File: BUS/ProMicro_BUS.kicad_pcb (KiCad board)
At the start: 2 copper layers, 17.8 x 30.5 mm, 17 parts, among them J1 Conn_01x03, U1 MAX3483, U2 MCP2515-xSO, U3 MAX3051, Y1 Crystal

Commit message: dump
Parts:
- removed the C1 at (53.3, 87.0)
- removed the C4 at (55.2, 87.0)
- removed C5, C6: 100n, Capacitor_SMD:C_0603_1608Metric
- added C2: 100n, Capacitor_SMD:C_0402_1005Metric, F.Cu at (55.2, 86.4)
- added C3: 10µ, Capacitor_SMD:C_0603_1608Metric, F.Cu at (53.3, 87.0)
- A1: value Sparkfun_Pro_Micro_3V3 -> Sparkfun_Pro_Micro
- moved LOGO1 10.4 mm to (59.1, 100.3), turned to 90 degrees
- moved JP3 2.57 mm to (57.2, 104.1)
- renumbered C2 to C1, C3 to C4, JP2 to JP1, JP1 to JP2, U3 to U2, U2 to U3
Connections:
- net D0 renamed TXD
- net D1 renamed RXD
- net D14 renamed CIPO
- net D15 renamed SCK
- net D16 renamed COPI
- net D7 renamed INT
- net D9 renamed CS1
- net Reset renamed ~RST
- A1 pad 13: (no net) -> CS0
- A1 pad 8: D5 -> (no net)
- JP3 pad 1: D5 -> CS0
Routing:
- net D5: track 24.1 -> 0.00 mm
- net CS0: track 0.00 -> 7.56 mm
- net CS1: track 2.51 -> 5.08 mm
- net CS: track 17.6 -> 16.6 mm
- net +3V3: track 26.1 -> 27.0 mm
- net GND: vias 26 -> 24
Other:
- board text added: "A"
- board text added: "B"
- board text added: "CIPO"
- board text added: "COPI"
- board text added: "CS0"
- board text added: "CS1"
- board text added: "G"
- board text added: "nerdyscout.github.io/ ProMicro/BUS v1.3"
- board text added: "~RST"
- board text removed: "CS"
- board text removed: "MISO"
- board text removed: "MOSI"
- board text removed: "RESET"
- board text removed: "TXDEN"
- board text removed: "nerdyscout.github.io/ProMicro/BUS"
- board text removed: "v1.2"

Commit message: clean
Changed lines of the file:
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@@
-(kicad_pcb (version 20171130) (host pcbnew 5.1.5)
+(kicad_pcb (version 20171130) (host pcbnew 5.1.5+dfsg1-2build2)
   (general
     (thickness 0.8)
     (drawings 24)
-    (tracks 178)
+    (tracks 179)
     (zones 0)
     (modules 15)
@@
       (effects (font (size 1 1) (thickness 0.15)))
     )
-    (pad 1 thru_hole rect (at 0 0) (size 1.6 1.6) (drill 0.8) (layers *.Cu *.Mask)
+    (pad 1 thru_hole rect (at 0 0) (size 2 2) (drill 1) (layers *.Cu *.Mask)
       (net 10 RXD))
-    (pad 2 thru_hole oval (at 0 2.54) (size 1.6 1.6) (drill 0.8) (layers *.Cu *.Mask)
+    (pad 2 thru_hole oval (at 0 2.54) (size 2 2) (drill 1) (layers *.Cu *.Mask)
       (net 11 TXD))
-    (pad 3 thru_hole oval (at 0 5.08) (size 1.6 1.6) (drill 0.8) (layers *.Cu *.Mask)
+    (pad 3 thru_hole oval (at 0 5.08) (size 2 2) (drill 1) (layers *.Cu *.Mask)
       (net 1 GND))
-    (pad 13 thru_hole oval (at 15.24 27.94) (size 1.6 1.6) (drill 0.8) (layers *.Cu *.Mask)
+    (pad 13 thru_hole oval (at 15.24 27.94) (size 2 2) (drill 1) (layers *.Cu *.Mask)
       (net 12 CS0))
-    (pad 4 thru_hole oval (at 0 7.62) (size 1.6 1.6) (drill 0.8) (layers *.Cu *.Mask)
+    (pad 4 thru_hole oval (at 0 7.62) (size 2 2) (drill 1) (layers *.Cu *.Mask)
       (net 1 GND))
-    (pad 14 thru_hole oval (at 15.24 25.4) (size 1.6 1.6) (drill 0.8) (layers *.Cu *.Mask)
+    (pad 14 thru_hole oval (at 15.24 25.4) (size 2 2) (drill 1) (layers *.Cu *.Mask)
       (net 13 COPI))
-    (pad 5 thru_hole oval (at 0 10.16) (size 1.6 1.6) (drill 0.8) (layers *.Cu *.Mask))
-    (pad 15 thru_hole oval (at 15.24 22.86) (size 1.6 1.6) (drill 0.8) (layers *.Cu *.Mask)
+    (pad 5 thru_hole oval (at 0 10.16) (size 2 2) (drill 1) (layers *.Cu *.Mask))
+    (pad 15 thru_hole oval (at 15.24 22.86) (size 2 2) (drill 1) (layers *.Cu *.Mask)
       (net 14 CIPO))
-    (pad 6 thru_hole oval (at 0 12.7) (size 1.6 1.6) (drill 0.8) (layers *.Cu *.Mask))
-    (pad 16 thru_hole oval (at 15.24 20.32) (size 1.6 1.6) (drill 0.8) (layers *.Cu *.Mask)
+    (pad 6 thru_hole oval (at 0 12.7) (size 2 2) (drill 1) (layers *.Cu *.Mask))
+    (pad 16 thru_hole oval (at 15.24 20.32) (size 2 2) (drill 1) (layers *.Cu *.Mask)
       (net 15 SCK))
-    (pad 7 thru_hole oval (at 0 15.24) (size 1.6 1.6) (drill 0.8) (layers *.Cu *.Mask))
-    (pad 17 thru_hole oval (at 15.24 17.78) (size 1.6 1.6) (drill 0.8) (layers *.Cu *.Mask))
-    (pad 8 thru_hole oval (at 0 17.78) (size 1.6 1.6) (drill 0.8) (layers *.Cu *.Mask))
-    (pad 18 thru_hole oval (at 15.24 15.24) (size 1.6 1.6) (drill 0.8) (layers *.Cu *.Mask))
-    (pad 9 thru_hole oval (at 0 20.32) (size 1.6 1.6) (drill 0.8) (layers *.Cu *.Mask))
-    (pad 19 thru_hole oval (at 15.24 12.7) (size 1.6 1.6) (drill 0.8) (layers *.Cu *.Mask))
-    (pad 10 thru_hole oval (at 0 22.86) (size 1.6 1.6) (drill 0.8) (layers *.Cu *.Mask)
+    (pad 7 thru_hole oval (at 0 15.24) (size 2 2) (drill 1) (layers *.Cu *.Mask))
+    (pad 17 thru_hole oval (at 15.24 17.78) (size 2 2) (drill 1) (layers *.Cu *.Mask))
+    (pad 8 thru_hole oval (at 0 17.78) (size 2 2) (drill 1) (layers *.Cu *.Mask))
+    (pad 18 thru_hole oval (at 15.24 15.24) (size 2 2) (drill 1) (layers *.Cu *.Mask))
+    (pad 9 thru_hole oval (at 0 20.32) (size 2 2) (drill 1) (layers *.Cu *.Mask))
+    (pad 19 thru_hole oval (at 15.24 12.7) (size 2 2) (drill 1) (layers *.Cu *.Mask))
+    (pad 10 thru_hole oval (at 0 22.86) (size 2 2) (drill 1) (layers *.Cu *.Mask)
       (net 16 INT))
-    (pad 20 thru_hole oval (at 15.24 10.16) (size 1.6 1.6) (drill 0.8) (layers *.Cu *.Mask))
-    (pad 11 thru_hole oval (at 0 25.4) (size 1.6 1.6) (drill 0.8) (layers *.Cu *.Mask))
-    (pad 21 thru_hole oval (at 15.24 7.62) (size 1.6 1.6) (drill 0.8) (layers *.Cu *.Mask)
+    (pad 20 thru_hole oval (at 15.24 10.16) (size 2 2) (drill 1) (layers *.Cu *.Mask))
+    (pad 11 thru_hole oval (at 0 25.4) (size 2 2) (drill 1) (layers *.Cu *.Mask))
+    (pad 21 thru_hole oval (at 15.24 7.62) (size 2 2) (drill 1) (layers *.Cu *.Mask)
       (net 2 +3V3))
-    (pad 12 thru_hole oval (at 0 27.94) (size 1.6 1.6) (drill 0.8) (layers *.Cu *.Mask)
+    (pad 12 thru_hole oval (at 0 27.94) (size 2 2) (drill 1) (layers *.Cu *.Mask)
       (net 17 CS1))
-    (pad 22 thru_hole oval (at 15.24 5.08) (size 1.6 1.6) (drill 0.8) (layers *.Cu *.Mask)
+    (pad 22 thru_hole oval (at 15.24 5.08) (size 2 2) (drill 1) (layers *.Cu *.Mask)
       (net 18 ~RST))
-    (pad 23 thru_hole oval (at 15.24 2.54) (size 1.6 1.6) (drill 0.8) (layers *.Cu *.Mask)
+    (pad 23 thru_hole oval (at 15.24 2.54) (size 2 2) (drill 1) (layers *.Cu *.Mask)
       (net 1 GND))
-    (pad 24 thru_hole oval (at 15.24 0) (size 1.6 1.6) (drill 0.8) (layers *.Cu *.Mask))
+    (pad 24 thru_hole oval (at 15.24 0) (size 2 2) (drill 1) (layers *.Cu *.Mask))
     (model ${KISYS3DMOD}/Module.3dshapes/Sparkfun_Pro_Micro.wrl
       (at (xyz 0 0 0))
@@
   (via (at 56.515 87.249) (size 0.6) (drill 0.3) (layers F.Cu B.Cu) (net 2))
   (segment (start 56.515 92.075) (end 56.515 87.249) (width 0.4) (layer B.Cu) (net 2))
-  (segment (start 60.556 87.48) (end 60.556 87.48) (width 0.4) (layer F.Cu) (net 2))
   (segment (start 55.245 87.7825) (end 54.2545 87.7825) (width 0.4) (layer F.Cu) (net 2))
   (segment (start 63.5 88.9) (end 63.5 88.9) (width 0.4) (layer F.Cu) (net 2))
@@
   (segment (start 62.507 87.757) (end 61.595 87.757) (width 0.4) (layer F.Cu) (net 2))
   (segment (start 62.507 87.757) (end 63.5 87.757) (width 0.4) (layer F.Cu) (net 2))
-  (segment (start 63.5 87.7825) (end 63.5 88.9) (width 0.4) (layer F.Cu) (net 2))
-  (segment (start 64.77 85.09) (end 66.04 83.82) (width 0.4) (layer F.Cu) (net 2))
-  (segment (start 64.2365 87.7825) (end 64.77 87.249) (width 0.4) (layer F.Cu) (net 2))
-  (segment (start 63.5 87.7825) (end 64.2365 87.7825) (width 0.4) (layer F.Cu) (net 2))
-  (segment (start 64.77 87.249) (end 64.77 85.09) (width 0.4) (layer F.Cu) (net 2))
   (via (at 60.579 87.249012) (size 0.6) (drill 0.3) (layers F.Cu B.Cu) (net 2))
   (segment (start 60.324988 86.995) (end 60.329001 86.999013) (width 0.4) (layer F.Cu) (net 2))
-  (segment (start 61.112488 87.7825) (end 60.579 87.249012) (width 0.4) (layer F.Cu) (net 2))
   (segment (start 58.7375 86.995) (end 60.324988 86.995) (width 0.4) (layer F.Cu) (net 2))
-  (segment (start 61.595 87.7825) (end 61.112488 87.7825) (width 0.4) (layer F.Cu) (net 2))
   (segment (start 60.329001 86.999013) (end 60.579 87.249012) (width 0.4) (layer F.Cu) (net 2))
   (segment (start 55.245 86.845) (end 55.245 86.995) (width 0.4) (layer F.Cu) (net 2))
   (segment (start 55.245 86.995) (end 55.245 87.7825) (width 0.4) (layer F.Cu) (net 2))
+  (segment (start 64.516 87.503) (end 64.516 85.344) (width 0.4) (layer F.Cu) (net 2))
+  (segment (start 64.262 87.757) (end 64.516 87.503) (width 0.4) (layer F.Cu) (net 2))
+  (segment (start 63.5 87.757) (end 64.262 87.757) (width 0.4) (layer F.Cu) (net 2))
+  (segment (start 64.516 85.344) (end 66.04 83.82) (width 0.4) (layer F.Cu) (net 2))
+  (segment (start 63.5 88.9) (end 63.5 87.757) (width 0.4) (layer F.Cu) (net 2))
+  (segment (start 61.086988 87.757) (end 60.579 87.249012) (width 0.4) (layer F.Cu) (net 2))
+  (segment (start 61.5695 87.757) (end 61.086988 87.757) (width 0.4) (layer F.Cu) (net 2))
   (segment (start 58.75 85.115) (end 58.75 85.895) (width 0.25) (layer F.Cu) (net 3))
   (segment (start 59.2075 83.82) (end 59.2075 84.6575) (width 0.25) (layer F.Cu) (net 3))
@@
   (segment (start 53.31 104.14) (end 50.8 104.14) (width 0.25) (layer B.Cu) (net 17))
   (segment (start 55.88 104.14) (end 53.31 104.14) (width 0.25) (layer B.Cu) (net 17))
-  (via (at 64.77 90.17) (size 0.5) (drill 0.2) (layers F.Cu B.Cu) (net 18))
-  (segment (start 64.77 90.17) (end 64.77 82.55) (width 0.25) (layer B.Cu) (net 18))
-  (segment (start 64.77 82.55) (end 66.04 81.28) (width 0.25) (layer B.Cu) (net 18))
-  (segment (start 64.77 91.059) (end 64.77 90.17) (width 0.25) (layer F.Cu) (net 18))
+  (via (at 64.515992 90.805) (size 0.5) (drill 0.2) (layers F.Cu B.Cu) (net 18))
+  (segment (start 66.04 81.28) (end 64.515992 82.804008) (width 0.25) (layer B.Cu) (net 18))
+  (segment (start 64.515992 82.804008) (end 64.515992 90.451447) (width 0.25) (layer B.Cu) (net 18))
+  (segment (start 64.515992 90.451447) (end 64.515992 90.805) (width 0.25) (layer B.Cu) (net 18))
+  (segment (start 64.515992 91.312992) (end 64.515992 90.805) (width 0.25) (layer F.Cu) (net 18))
+  (segment (start 64.516 91.313) (end 64.515992 91.312992) (width 0.25) (layer F.Cu) (net 18))
+  (segment (start 64.389 91.44) (end 64.516 91.313) (width 0.25) (layer F.Cu) (net 18))
   (segment (start 63.07 91.44) (end 64.389 91.44) (width 0.25) (layer F.Cu) (net 18))
-  (segment (start 64.389 91.44) (end 64.77 91.059) (width 0.25) (layer F.Cu) (net 18))
   (segment (start 56.57 103.378) (end 54.483 103.378) (width 0.25) (layer F.Cu) (net 19))
   (segment (start 53.77 99.06) (end 55.372 99.06) (width 0.25) (layer F.Cu) (net 19))

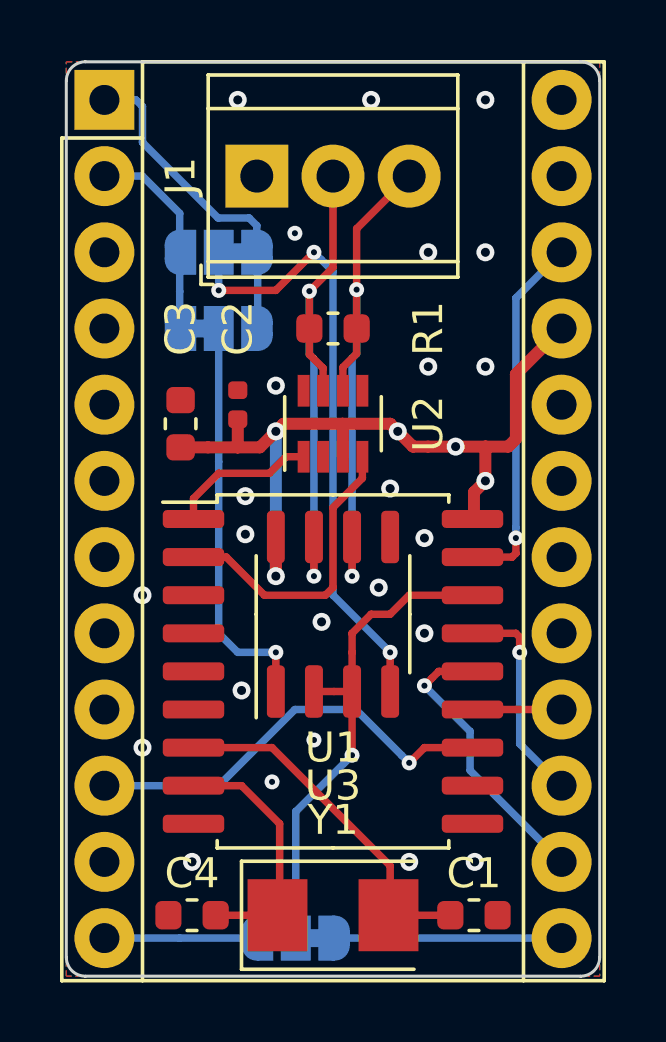
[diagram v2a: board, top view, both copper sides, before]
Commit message: make controller holes wide enough
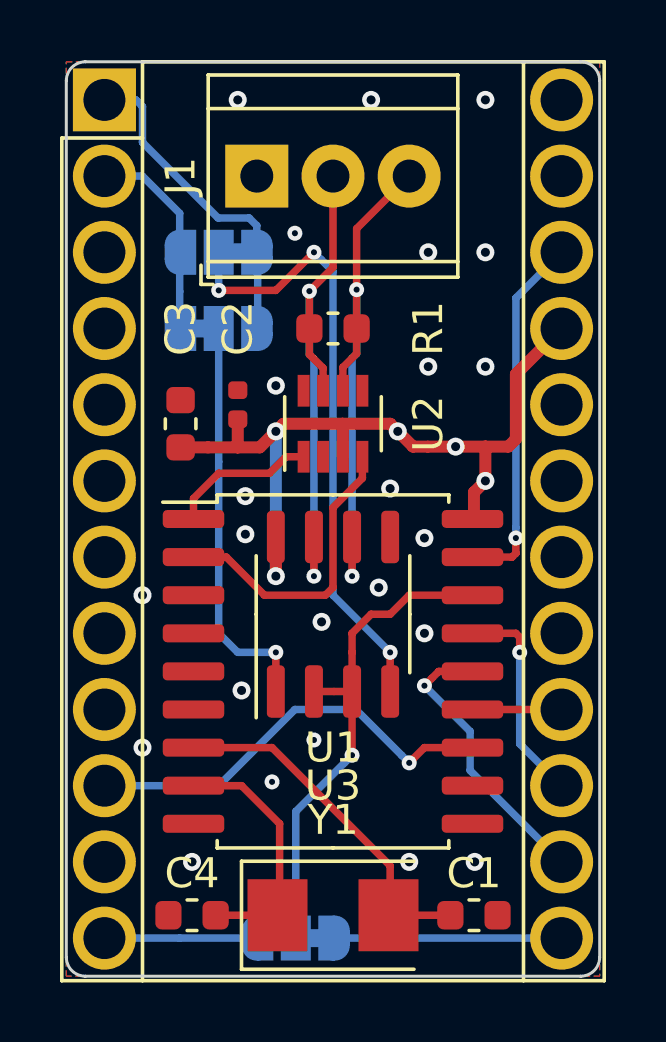
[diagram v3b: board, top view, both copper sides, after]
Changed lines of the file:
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@@
-(kicad_pcb (version 20171130) (host pcbnew 5.1.5+dfsg1-2build2)
+(kicad_pcb (version 20171130) (host pcbnew 5.1.5)
   (general
     (thickness 0.8)
@@
       (effects (font (size 1 1) (thickness 0.15)))
     )
-    (pad 1 thru_hole rect (at 0 0) (size 2 2) (drill 1) (layers *.Cu *.Mask)
+    (pad 1 thru_hole rect (at 0 0) (size 2.1 2.1) (drill 1.4) (layers *.Cu *.Mask)
       (net 10 RXD))
-    (pad 2 thru_hole oval (at 0 2.54) (size 2 2) (drill 1) (layers *.Cu *.Mask)
+    (pad 2 thru_hole circle (at 0 2.54) (size 2.1 2.1) (drill 1.4) (layers *.Cu *.Mask)
       (net 11 TXD))
-    (pad 3 thru_hole oval (at 0 5.08) (size 2 2) (drill 1) (layers *.Cu *.Mask)
-      (net 1 GND))
-    (pad 13 thru_hole oval (at 15.24 27.94) (size 2 2) (drill 1) (layers *.Cu *.Mask)
+    (pad 3 thru_hole circle (at 0 5.08) (size 2.1 2.1) (drill 1.4) (layers *.Cu *.Mask)
+      (net 1 GND))
+    (pad 13 thru_hole circle (at 15.24 27.94) (size 2.1 2.1) (drill 1.4) (layers *.Cu *.Mask)
       (net 12 CS0))
-    (pad 4 thru_hole oval (at 0 7.62) (size 2 2) (drill 1) (layers *.Cu *.Mask)
-      (net 1 GND))
-    (pad 14 thru_hole oval (at 15.24 25.4) (size 2 2) (drill 1) (layers *.Cu *.Mask)
+    (pad 4 thru_hole circle (at 0 7.62) (size 2.1 2.1) (drill 1.4) (layers *.Cu *.Mask)
+      (net 1 GND))
+    (pad 14 thru_hole circle (at 15.24 25.4) (size 2.1 2.1) (drill 1.4) (layers *.Cu *.Mask)
       (net 13 COPI))
-    (pad 5 thru_hole oval (at 0 10.16) (size 2 2) (drill 1) (layers *.Cu *.Mask))
-    (pad 15 thru_hole oval (at 15.24 22.86) (size 2 2) (drill 1) (layers *.Cu *.Mask)
+    (pad 5 thru_hole circle (at 0 10.16) (size 2.1 2.1) (drill 1.4) (layers *.Cu *.Mask))
+    (pad 15 thru_hole circle (at 15.24 22.86) (size 2.1 2.1) (drill 1.4) (layers *.Cu *.Mask)
       (net 14 CIPO))
-    (pad 6 thru_hole oval (at 0 12.7) (size 2 2) (drill 1) (layers *.Cu *.Mask))
-    (pad 16 thru_hole oval (at 15.24 20.32) (size 2 2) (drill 1) (layers *.Cu *.Mask)
+    (pad 6 thru_hole circle (at 0 12.7) (size 2.1 2.1) (drill 1.4) (layers *.Cu *.Mask))
+    (pad 16 thru_hole circle (at 15.24 20.32) (size 2.1 2.1) (drill 1.4) (layers *.Cu *.Mask)
       (net 15 SCK))
-    (pad 7 thru_hole oval (at 0 15.24) (size 2 2) (drill 1) (layers *.Cu *.Mask))
-    (pad 17 thru_hole oval (at 15.24 17.78) (size 2 2) (drill 1) (layers *.Cu *.Mask))
-    (pad 8 thru_hole oval (at 0 17.78) (size 2 2) (drill 1) (layers *.Cu *.Mask))
-    (pad 18 thru_hole oval (at 15.24 15.24) (size 2 2) (drill 1) (layers *.Cu *.Mask))
-    (pad 9 thru_hole oval (at 0 20.32) (size 2 2) (drill 1) (layers *.Cu *.Mask))
-    (pad 19 thru_hole oval (at 15.24 12.7) (size 2 2) (drill 1) (layers *.Cu *.Mask))
-    (pad 10 thru_hole oval (at 0 22.86) (size 2 2) (drill 1) (layers *.Cu *.Mask)
+    (pad 7 thru_hole circle (at 0 15.24) (size 2.1 2.1) (drill 1.4) (layers *.Cu *.Mask))
+    (pad 17 thru_hole circle (at 15.24 17.78) (size 2.1 2.1) (drill 1.4) (layers *.Cu *.Mask))
+    (pad 8 thru_hole circle (at 0 17.78) (size 2.1 2.1) (drill 1.4) (layers *.Cu *.Mask))
+    (pad 18 thru_hole circle (at 15.24 15.24) (size 2.1 2.1) (drill 1.4) (layers *.Cu *.Mask))
+    (pad 9 thru_hole circle (at 0 20.32) (size 2.1 2.1) (drill 1.4) (layers *.Cu *.Mask))
+    (pad 19 thru_hole circle (at 15.24 12.7) (size 2.1 2.1) (drill 1.4) (layers *.Cu *.Mask))
+    (pad 10 thru_hole circle (at 0 22.86) (size 2.1 2.1) (drill 1.4) (layers *.Cu *.Mask)
       (net 16 INT))
-    (pad 20 thru_hole oval (at 15.24 10.16) (size 2 2) (drill 1) (layers *.Cu *.Mask))
-    (pad 11 thru_hole oval (at 0 25.4) (size 2 2) (drill 1) (layers *.Cu *.Mask))
-    (pad 21 thru_hole oval (at 15.24 7.62) (size 2 2) (drill 1) (layers *.Cu *.Mask)
+    (pad 20 thru_hole circle (at 15.24 10.16) (size 2.1 2.1) (drill 1.4) (layers *.Cu *.Mask))
+    (pad 11 thru_hole circle (at 0 25.4) (size 2.1 2.1) (drill 1.4) (layers *.Cu *.Mask))
+    (pad 21 thru_hole circle (at 15.24 7.62) (size 2.1 2.1) (drill 1.4) (layers *.Cu *.Mask)
       (net 2 +3V3))
-    (pad 12 thru_hole oval (at 0 27.94) (size 2 2) (drill 1) (layers *.Cu *.Mask)
+    (pad 12 thru_hole circle (at 0 27.94) (size 2.1 2.1) (drill 1.4) (layers *.Cu *.Mask)
       (net 17 CS1))
-    (pad 22 thru_hole oval (at 15.24 5.08) (size 2 2) (drill 1) (layers *.Cu *.Mask)
+    (pad 22 thru_hole circle (at 15.24 5.08) (size 2.1 2.1) (drill 1.4) (layers *.Cu *.Mask)
       (net 18 ~RST))
-    (pad 23 thru_hole oval (at 15.24 2.54) (size 2 2) (drill 1) (layers *.Cu *.Mask)
-      (net 1 GND))
-    (pad 24 thru_hole oval (at 15.24 0) (size 2 2) (drill 1) (layers *.Cu *.Mask))
+    (pad 23 thru_hole circle (at 15.24 2.54) (size 2.1 2.1) (drill 1.4) (layers *.Cu *.Mask)
+      (net 1 GND))
+    (pad 24 thru_hole circle (at 15.24 0) (size 2.1 2.1) (drill 1.4) (layers *.Cu *.Mask))
     (model ${KISYS3DMOD}/Module.3dshapes/Sparkfun_Pro_Micro.wrl
       (at (xyz 0 0 0))
